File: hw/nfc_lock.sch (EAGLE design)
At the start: 32 parts, among them IC1 STM8S003F3, IC3 MCP170312MB, Q1 8MHz, Q3 2N7002,215, U1 M24SR16-YMN6T/2, U2 2N7002,215, U3 2N7002,215, U4 IRFML8244TRPBF, X1 MINI-USB-32005-301

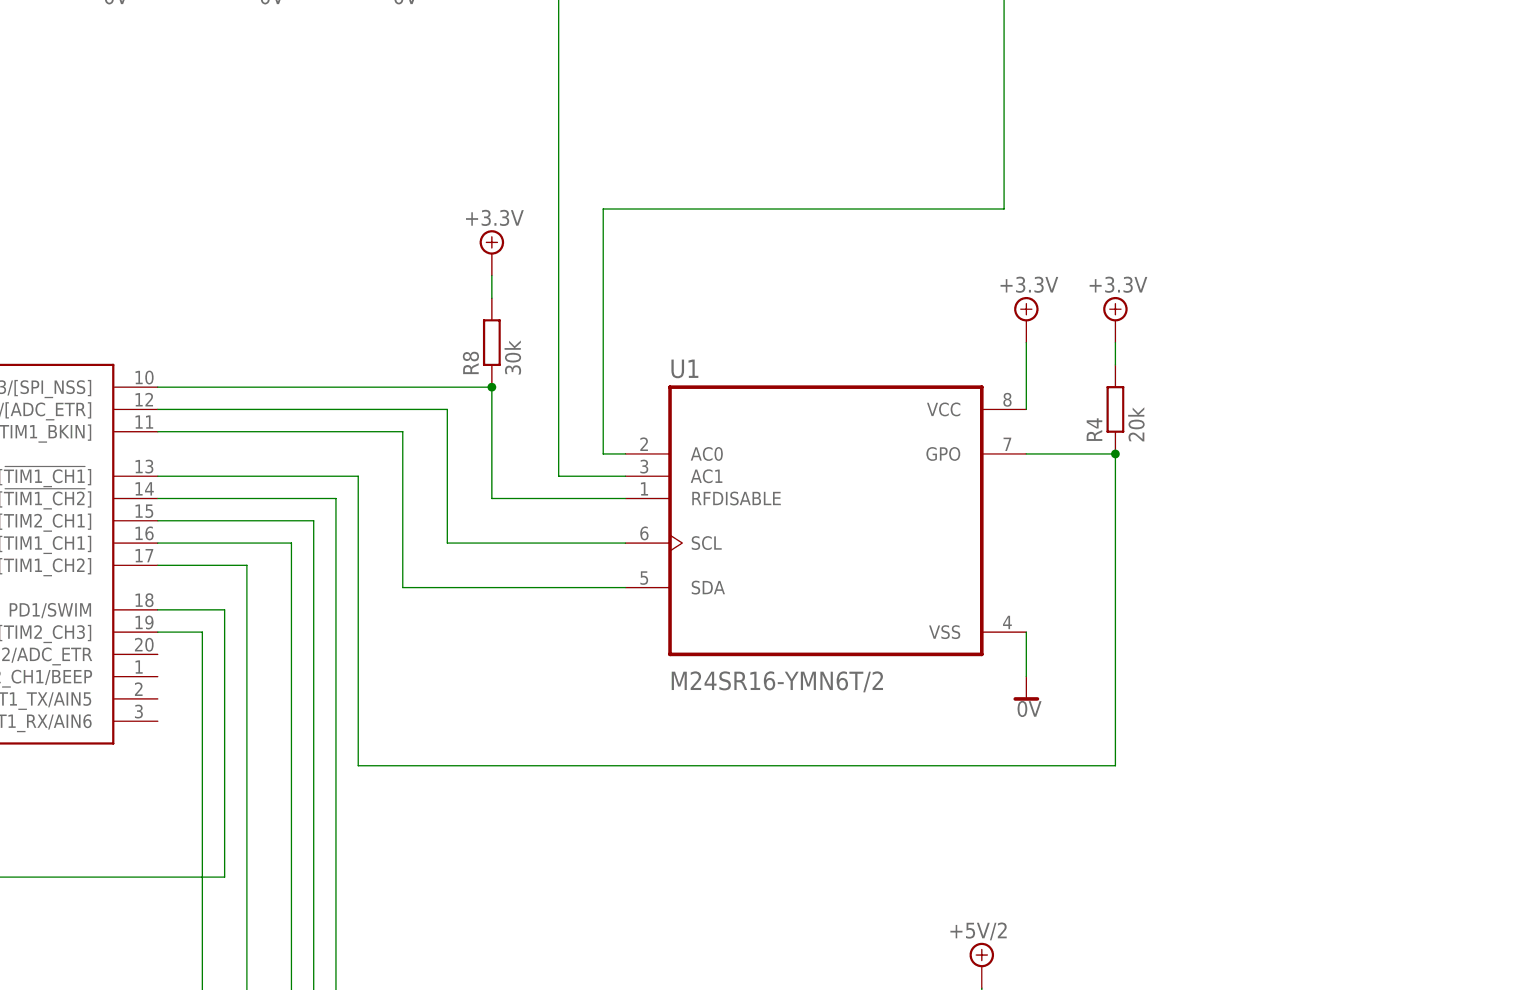
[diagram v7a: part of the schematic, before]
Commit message: added pull-ups for I2C and m24sr Vcc decoupling; changed antena type to single-sided
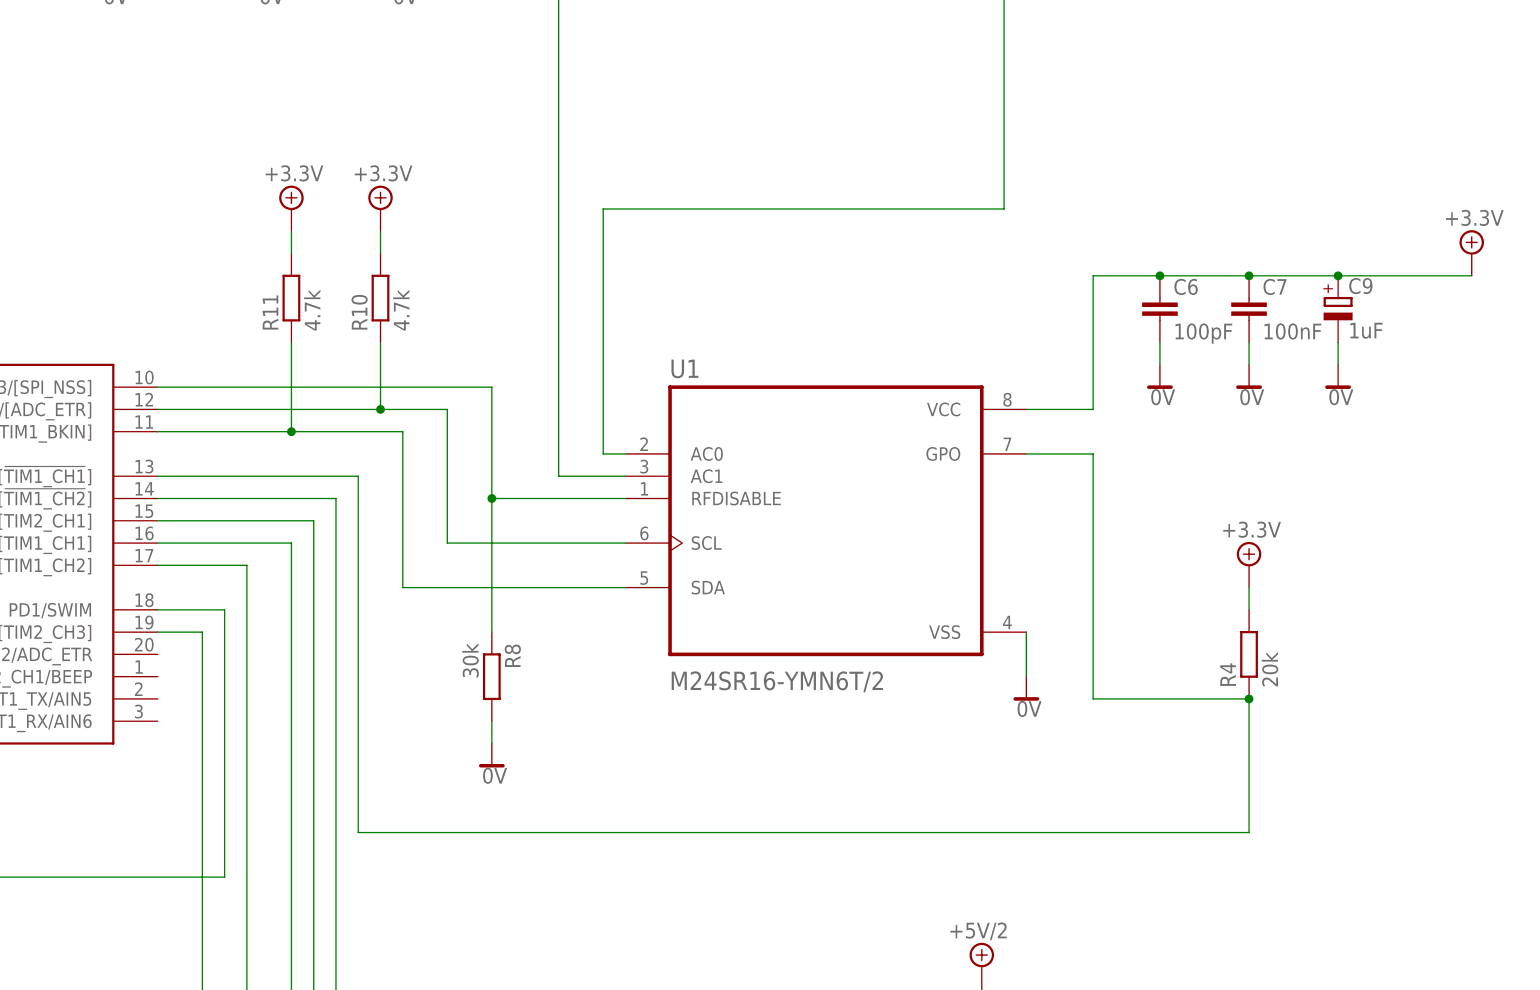
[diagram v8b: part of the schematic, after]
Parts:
- added C6: 100pF, rcl:C-EUC1206
- added C7: 100nF, rcl:C-EUC1206
- added C9: 1uF, rcl:CPOL-EU153CLV-0405
- added R10, R11: 4.7k, rcl:R-EU_R0805
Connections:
- net +5V/1: now also C6.1, C7.1, C9.+, R10.2, R11.2; no longer R8.2
- net 0V: now also C6.2, C7.2, C9.-, R8.2
- net SCL: now also R10.1
- net SDA: now also R11.1
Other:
- moved on the sheet: R4, R8
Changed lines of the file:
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@@
 <part name="SUPPLY32" library="supply2" deviceset="+5V/2" device=""/>
 <part name="R8" library="rcl" deviceset="R-EU_" device="R0805" value="30k"/>
-<part name="SUPPLY33" library="supply2" deviceset="+5V/1" device="" value="+3.3V"/>
 <part name="SV4" library="con-lstb" deviceset="MA03-1" device="" value="SERVO#4"/>
 <part name="SV5" library="con-lstb" deviceset="MA03-1" device="" value="SERVO#2"/>
@@
 <part name="SUPPLY38" library="supply2" deviceset="0V" device=""/>
 <part name="SUPPLY39" library="supply2" deviceset="0V" device=""/>
+<part name="C6" library="rcl" deviceset="C-EU" device="C1206" value="100pF"/>
+<part name="C7" library="rcl" deviceset="C-EU" device="C1206" value="100nF"/>
+<part name="C9" library="rcl" deviceset="CPOL-EU" device="153CLV-0405" value="1uF"/>
+<part name="R10" library="rcl" deviceset="R-EU_" device="R0805" value="4.7k"/>
+<part name="R11" library="rcl" deviceset="R-EU_" device="R0805" value="4.7k"/>
+<part name="SUPPLY23" library="supply2" deviceset="+5V/1" device="" value="+3.3V"/>
+<part name="SUPPLY24" library="supply2" deviceset="+5V/1" device="" value="+3.3V"/>
+<part name="SUPPLY33" library="supply2" deviceset="0V" device=""/>
+<part name="SUPPLY34" library="supply2" deviceset="0V" device=""/>
+<part name="SUPPLY37" library="supply2" deviceset="0V" device=""/>
+<part name="SUPPLY40" library="supply2" deviceset="0V" device=""/>
 </parts>
 <sheets>
@@
 <instance part="SUPPLY9" gate="0V" x="-10.16" y="68.58"/>
 <instance part="SUPPLY10" gate="0V" x="157.48" y="58.42"/>
-<instance part="SUPPLY11" gate="G$1" x="157.48" y="101.6"/>
+<instance part="SUPPLY11" gate="G$1" x="208.28" y="109.22"/>
 <instance part="R1" gate="G$1" x="-43.18" y="106.68" rot="R270"/>
 <instance part="C1" gate="G$1" x="-43.18" y="91.44"/>
@@
 <instance part="SUPPLY21" gate="0V" x="-63.5" y="93.98"/>
 <instance part="SV3" gate="G$1" x="-124.46" y="20.32"/>
-<instance part="R4" gate="G$1" x="167.64" y="91.44" rot="R90"/>
-<instance part="SUPPLY25" gate="G$1" x="167.64" y="101.6"/>
+<instance part="R4" gate="G$1" x="182.88" y="63.5" rot="R90"/>
+<instance part="SUPPLY25" gate="G$1" x="182.88" y="73.66"/>
 <instance part="LED1" gate="G$1" x="152.4" y="20.32"/>
 <instance part="R5" gate="G$1" x="152.4" y="7.62" rot="R270"/>
@@
 <instance part="SUPPLY22" gate="G$1" x="152.4" y="27.94"/>
 <instance part="SUPPLY32" gate="G$1" x="99.06" y="-30.48"/>
-<instance part="R8" gate="G$1" x="96.52" y="99.06" rot="R90"/>
-<instance part="SUPPLY33" gate="G$1" x="96.52" y="109.22"/>
+<instance part="R8" gate="G$1" x="96.52" y="60.96" rot="R270"/>
 <instance part="SV4" gate="G$1" x="-137.16" y="20.32"/>
 <instance part="SV5" gate="G$1" x="-137.16" y="-25.4"/>
@@
 <instance part="SUPPLY38" gate="0V" x="-50.8" y="-99.06"/>
 <instance part="SUPPLY39" gate="0V" x="-71.12" y="-99.06"/>
+<instance part="C6" gate="G$1" x="172.72" y="104.14"/>
+<instance part="C7" gate="G$1" x="182.88" y="104.14"/>
+<instance part="C9" gate="G$1" x="193.04" y="104.14"/>
+<instance part="R10" gate="G$1" x="83.82" y="104.14" rot="R90"/>
+<instance part="R11" gate="G$1" x="73.66" y="104.14" rot="R90"/>
+<instance part="SUPPLY23" gate="G$1" x="83.82" y="114.3"/>
+<instance part="SUPPLY24" gate="G$1" x="73.66" y="114.3"/>
+<instance part="SUPPLY33" gate="0V" x="96.52" y="50.8"/>
+<instance part="SUPPLY34" gate="0V" x="172.72" y="93.98"/>
+<instance part="SUPPLY37" gate="0V" x="182.88" y="93.98"/>
+<instance part="SUPPLY40" gate="0V" x="193.04" y="93.98"/>
 </instances>
 <busses>
@@
 <segment>
 <pinref part="IC1" gate="G$1" pin="PB4/I2C_SCL/[ADC_ETR]"/>
-<wire x1="58.42" y1="91.44" x2="91.44" y2="91.44" width="0.1524" layer="91"/>
+<wire x1="58.42" y1="91.44" x2="83.82" y2="91.44" width="0.1524" layer="91"/>
+<wire x1="83.82" y1="91.44" x2="91.44" y2="91.44" width="0.1524" layer="91"/>
 <wire x1="91.44" y1="91.44" x2="91.44" y2="76.2" width="0.1524" layer="91"/>
 <pinref part="U1" gate="G$1" pin="SCL"/>
 <wire x1="91.44" y1="76.2" x2="111.76" y2="76.2" width="0.1524" layer="91"/>
+<pinref part="R10" gate="G$1" pin="1"/>
+<wire x1="83.82" y1="99.06" x2="83.82" y2="91.44" width="0.1524" layer="91"/>
+<junction x="83.82" y="91.44"/>
 </segment>
 </net>
@@
 <segment>
 <pinref part="IC1" gate="G$1" pin="PB5/I2C_SDA/[TIM1_BKIN]"/>
-<wire x1="58.42" y1="88.9" x2="86.36" y2="88.9" width="0.1524" layer="91"/>
+<wire x1="58.42" y1="88.9" x2="73.66" y2="88.9" width="0.1524" layer="91"/>
+<wire x1="73.66" y1="88.9" x2="86.36" y2="88.9" width="0.1524" layer="91"/>
 <wire x1="86.36" y1="88.9" x2="86.36" y2="71.12" width="0.1524" layer="91"/>
 <pinref part="U1" gate="G$1" pin="SDA"/>
 <wire x1="86.36" y1="71.12" x2="111.76" y2="71.12" width="0.1524" layer="91"/>
+<pinref part="R11" gate="G$1" pin="1"/>
+<wire x1="73.66" y1="99.06" x2="73.66" y2="88.9" width="0.1524" layer="91"/>
+<junction x="73.66" y="88.9"/>
 </segment>
 </net>
@@
 <pinref part="SUPPLY38" gate="0V" pin="0V"/>
 <wire x1="-50.8" y1="-96.52" x2="-50.8" y2="-88.9" width="0.1524" layer="91"/>
+</segment>
+<segment>
+<pinref part="R8" gate="G$1" pin="2"/>
+<pinref part="SUPPLY33" gate="0V" pin="0V"/>
+<wire x1="96.52" y1="53.34" x2="96.52" y2="55.88" width="0.1524" layer="91"/>
+</segment>
+<segment>
+<pinref part="C6" gate="G$1" pin="2"/>
+<pinref part="SUPPLY34" gate="0V" pin="0V"/>
+<wire x1="172.72" y1="96.52" x2="172.72" y2="99.06" width="0.1524" layer="91"/>
+</segment>
+<segment>
+<pinref part="C7" gate="G$1" pin="2"/>
+<pinref part="SUPPLY37" gate="0V" pin="0V"/>
+<wire x1="182.88" y1="96.52" x2="182.88" y2="99.06" width="0.1524" layer="91"/>
+</segment>
+<segment>
+<pinref part="C9" gate="G$1" pin="-"/>
+<pinref part="SUPPLY40" gate="0V" pin="0V"/>
+<wire x1="193.04" y1="96.52" x2="193.04" y2="99.06" width="0.1524" layer="91"/>
 </segment>
 </net>
@@
 <pinref part="U1" gate="G$1" pin="VCC"/>
 <pinref part="SUPPLY11" gate="G$1" pin="+5V/1"/>
-<wire x1="157.48" y1="99.06" x2="157.48" y2="91.44" width="0.1524" layer="91"/>
+<wire x1="208.28" y1="106.68" x2="193.04" y2="106.68" width="0.1524" layer="91"/>
+<wire x1="193.04" y1="106.68" x2="182.88" y2="106.68" width="0.1524" layer="91"/>
+<wire x1="182.88" y1="106.68" x2="172.72" y2="106.68" width="0.1524" layer="91"/>
+<wire x1="172.72" y1="106.68" x2="165.1" y2="106.68" width="0.1524" layer="91"/>
+<wire x1="165.1" y1="106.68" x2="165.1" y2="91.44" width="0.1524" layer="91"/>
+<wire x1="165.1" y1="91.44" x2="157.48" y2="91.44" width="0.1524" layer="91"/>
+<pinref part="C6" gate="G$1" pin="1"/>
+<junction x="172.72" y="106.68"/>
+<pinref part="C7" gate="G$1" pin="1"/>
+<junction x="182.88" y="106.68"/>
+<pinref part="C9" gate="G$1" pin="+"/>
+<junction x="193.04" y="106.68"/>
 </segment>
 <segment>
@@
 <pinref part="R4" gate="G$1" pin="2"/>
 <pinref part="SUPPLY25" gate="G$1" pin="+5V/1"/>
-<wire x1="167.64" y1="99.06" x2="167.64" y2="96.52" width="0.1524" layer="91"/>
-</segment>
-<segment>
-<pinref part="R8" gate="G$1" pin="2"/>
-<pinref part="SUPPLY33" gate="G$1" pin="+5V/1"/>
-<wire x1="96.52" y1="106.68" x2="96.52" y2="104.14" width="0.1524" layer="91"/>
+<wire x1="182.88" y1="71.12" x2="182.88" y2="68.58" width="0.1524" layer="91"/>
+</segment>
+<segment>
+<pinref part="R10" gate="G$1" pin="2"/>
+<pinref part="SUPPLY23" gate="G$1" pin="+5V/1"/>
+<wire x1="83.82" y1="111.76" x2="83.82" y2="109.22" width="0.1524" layer="91"/>
+</segment>
+<segment>
+<pinref part="R11" gate="G$1" pin="2"/>
+<pinref part="SUPPLY24" gate="G$1" pin="+5V/1"/>
+<wire x1="73.66" y1="111.76" x2="73.66" y2="109.22" width="0.1524" layer="91"/>
 </segment>
 </net>
@@
 <net name="N$7" class="0">
 <segment>
+<wire x1="96.52" y1="66.04" x2="96.52" y2="81.28" width="0.1524" layer="91"/>
+<pinref part="U1" gate="G$1" pin="RFDISABLE"/>
+<wire x1="96.52" y1="81.28" x2="111.76" y2="81.28" width="0.1524" layer="91"/>
+<pinref part="R8" gate="G$1" pin="1"/>
 <pinref part="IC1" gate="G$1" pin="PA3/TIM2_CH3/[SPI_NSS]"/>
 <wire x1="58.42" y1="93.98" x2="96.52" y2="93.98" width="0.1524" layer="91"/>
 <wire x1="96.52" y1="93.98" x2="96.52" y2="81.28" width="0.1524" layer="91"/>
-<pinref part="U1" gate="G$1" pin="RFDISABLE"/>
-<wire x1="96.52" y1="81.28" x2="111.76" y2="81.28" width="0.1524" layer="91"/>
-<pinref part="R8" gate="G$1" pin="1"/>
-<junction x="96.52" y="93.98"/>
+<junction x="96.52" y="81.28"/>
 </segment>
 </net>
@@
 <pinref part="IC1" gate="G$1" pin="PC3/TIM1_CH3/[TLI]/[!TIM1_CH1!]"/>
 <wire x1="58.42" y1="83.82" x2="81.28" y2="83.82" width="0.1524" layer="91"/>
-<wire x1="81.28" y1="83.82" x2="81.28" y2="50.8" width="0.1524" layer="91"/>
-<wire x1="81.28" y1="50.8" x2="167.64" y2="50.8" width="0.1524" layer="91"/>
-<wire x1="167.64" y1="50.8" x2="167.64" y2="86.36" width="0.1524" layer="91"/>
+<wire x1="81.28" y1="83.82" x2="81.28" y2="43.18" width="0.1524" layer="91"/>
+<wire x1="81.28" y1="43.18" x2="182.88" y2="43.18" width="0.1524" layer="91"/>
+<wire x1="182.88" y1="43.18" x2="182.88" y2="58.42" width="0.1524" layer="91"/>
 <pinref part="U1" gate="G$1" pin="GPO"/>
-<wire x1="167.64" y1="86.36" x2="157.48" y2="86.36" width="0.1524" layer="91"/>
+<wire x1="182.88" y1="58.42" x2="165.1" y2="58.42" width="0.1524" layer="91"/>
+<wire x1="165.1" y1="58.42" x2="165.1" y2="86.36" width="0.1524" layer="91"/>
+<wire x1="165.1" y1="86.36" x2="157.48" y2="86.36" width="0.1524" layer="91"/>
 <pinref part="R4" gate="G$1" pin="1"/>
-<junction x="167.64" y="86.36"/>
-</segment>
-</net>
+<junction x="182.88" y="58.42"/>
+</segment>
+</net>
